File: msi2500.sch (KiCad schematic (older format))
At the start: 23 parts, among them J1 VCC_GPIO, J2 GPIO0, J3 GPIO1, J4 GPIO2, J5 GPIO3, U1 msi2500, Y1 24MHz, Y2 24MHZ

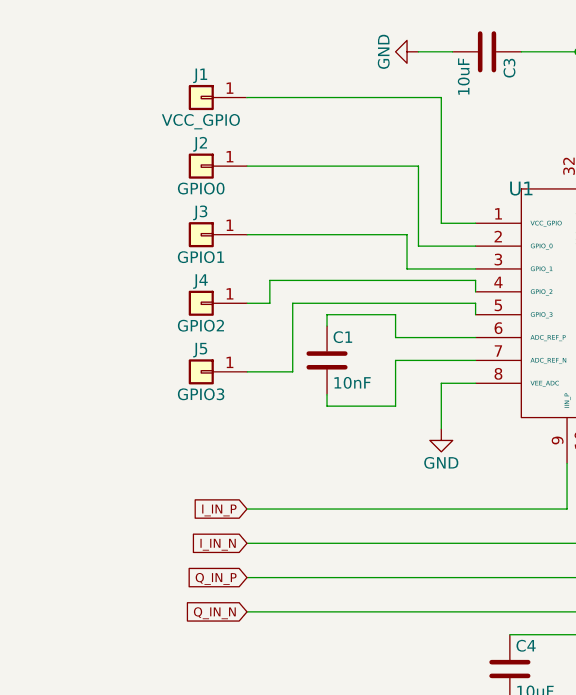
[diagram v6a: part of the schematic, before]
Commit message: add gpio pull down res
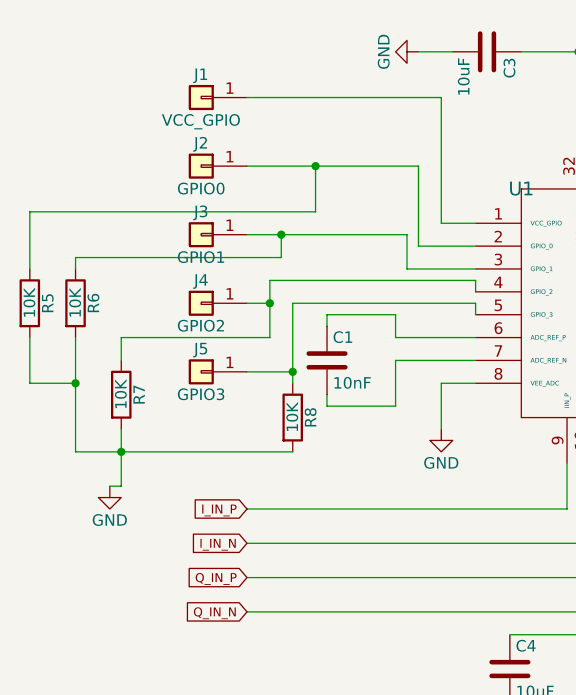
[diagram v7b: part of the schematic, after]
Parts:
- added R5, R6, R7, R8: 10K, Resistors_SMD:R_0603, symbol R
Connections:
- net GND: now also R5.2, R6.2, R7.2, R8.2
- net at J2.1 (Pin_1), U1.2 (GPIO_0): now also R5.1
- net at J3.1 (Pin_1), U1.3 (GPIO_1): now also R6.1
- net at J4.1 (Pin_1), U1.4 (GPIO_2): now also R7.1
- net at J5.1 (Pin_1), U1.5 (GPIO_3): now also R8.1
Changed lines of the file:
@@
 $EndDescr
 $Comp
-L GND #PWR5
+L GND #PWR6
 U 1 1 5C68D20C
 P 5450 2800
-F 0 "#PWR5" H 5450 2550 50  0001 C CNN
+F 0 "#PWR6" H 5450 2550 50  0001 C CNN
 F 1 "GND" H 5450 2650 50  0000 C CNN
 F 2 "" H 5450 2800 50  0001 C CNN
@@
 $EndComp
 $Comp
-L GND #PWR8
+L GND #PWR9
 U 1 1 5C68D2D4
 P 5900 4750
-F 0 "#PWR8" H 5900 4500 50  0001 C CNN
+F 0 "#PWR9" H 5900 4500 50  0001 C CNN
 F 1 "GND" H 5900 4600 50  0000 C CNN
 F 2 "" H 5900 4750 50  0001 C CNN
@@
 	4350 3950 4050 3950
 $Comp
-L GND #PWR3
+L GND #PWR4
 U 1 1 5C68D520
 P 4550 4450
-F 0 "#PWR3" H 4550 4200 50  0001 C CNN
+F 0 "#PWR4" H 4550 4200 50  0001 C CNN
 F 1 "GND" H 4550 4300 50  0000 C CNN
 F 2 "" H 4550 4450 50  0001 C CNN
@@
 	5800 5100 6950 5100
 $Comp
-L GND #PWR4
+L GND #PWR5
 U 1 1 5C68D665
 P 4850 5850
-F 0 "#PWR4" H 4850 5600 50  0001 C CNN
+F 0 "#PWR5" H 4850 5600 50  0001 C CNN
 F 1 "GND" H 4850 5700 50  0000 C CNN
 F 2 "" H 4850 5850 50  0001 C CNN
@@
 $EndComp
 $Comp
-L GND #PWR11
+L GND #PWR12
 U 1 1 5C68D681
 P 6950 5800
-F 0 "#PWR11" H 6950 5550 50  0001 C CNN
+F 0 "#PWR12" H 6950 5550 50  0001 C CNN
 F 1 "GND" H 6950 5650 50  0000 C CNN
 F 2 "" H 6950 5800 50  0001 C CNN
@@
 Connection ~ 5800 5600
 $Comp
-L GND #PWR6
+L GND #PWR7
 U 1 1 5C68DAB6
 P 5500 6150
-F 0 "#PWR6" H 5500 5900 50  0001 C CNN
+F 0 "#PWR7" H 5500 5900 50  0001 C CNN
 F 1 "GND" H 5500 6000 50  0000 C CNN
 F 2 "" H 5500 6150 50  0001 C CNN
@@
 $EndComp
 $Comp
-L GND #PWR7
+L GND #PWR8
 U 1 1 5C68DAD6
 P 5800 6150
-F 0 "#PWR7" H 5800 5900 50  0001 C CNN
+F 0 "#PWR8" H 5800 5900 50  0001 C CNN
 F 1 "GND" H 5800 6000 50  0000 C CNN
 F 2 "" H 5800 6150 50  0001 C CNN
@@
 VDIG
 $Comp
-L GND #PWR9
+L GND #PWR10
 U 1 1 5C68DD59
 P 6500 4700
-F 0 "#PWR9" H 6500 4450 50  0001 C CNN
+F 0 "#PWR10" H 6500 4450 50  0001 C CNN
 F 1 "GND" H 6500 4550 50  0000 C CNN
 F 2 "" H 6500 4700 50  0001 C CNN
@@
 $EndComp
 $Comp
-L GND #PWR10
+L GND #PWR11
 U 1 1 5C68DD79
 P 6800 4650
-F 0 "#PWR10" H 6800 4400 50  0001 C CNN
+F 0 "#PWR11" H 6800 4400 50  0001 C CNN
 F 1 "GND" H 6800 4500 50  0000 C CNN
 F 2 "" H 6800 4650 50  0001 C CNN
@@
 	6250 3950 7000 3950
 $Comp
-L GND #PWR12
+L GND #PWR13
 U 1 1 5C68E182
 P 7300 3800
-F 0 "#PWR12" H 7300 3550 50  0001 C CNN
+F 0 "#PWR13" H 7300 3550 50  0001 C CNN
 F 1 "GND" H 7300 3650 50  0000 C CNN
 F 2 "" H 7300 3800 50  0001 C CNN
@@
 $EndComp
 $Comp
-L GND #PWR14
+L GND #PWR15
 U 1 1 5C68E538
 P 7850 3200
-F 0 "#PWR14" H 7850 2950 50  0001 C CNN
+F 0 "#PWR15" H 7850 2950 50  0001 C CNN
 F 1 "GND" H 7850 3050 50  0000 C CNN
 F 2 "" H 7850 3200 50  0001 C CNN
@@
 $EndComp
 $Comp
-L GND #PWR15
+L GND #PWR16
 U 1 1 5C68E5AE
 P 7850 3600
-F 0 "#PWR15" H 7850 3350 50  0001 C CNN
+F 0 "#PWR16" H 7850 3350 50  0001 C CNN
 F 1 "GND" H 7850 3450 50  0000 C CNN
 F 2 "" H 7850 3600 50  0001 C CNN
@@
 Connection ~ 7100 3600
 $Comp
-L GND #PWR2
+L GND #PWR3
 U 1 1 5C68EA62
 P 4450 2800
-F 0 "#PWR2" H 4450 2550 50  0001 C CNN
+F 0 "#PWR3" H 4450 2550 50  0001 C CNN
 F 1 "GND" H 4450 2650 50  0000 C CNN
 F 2 "" H 4450 2800 50  0001 C CNN
@@
 $EndComp
 $Comp
-L GND #PWR1
+L GND #PWR2
 U 1 1 5C68F152
 P 4450 2050
-F 0 "#PWR1" H 4450 1800 50  0001 C CNN
+F 0 "#PWR2" H 4450 1800 50  0001 C CNN
 F 1 "GND" H 4450 1900 50  0000 C CNN
 F 2 "" H 4450 2050 50  0001 C CNN
@@
 	3700 3900 3800 3900
 Wire Wire Line
-	3800 3900 3800 3800
+	3800 3800 3800 4050
 Wire Wire Line
 	3800 3800 4700 3800
@@
 	4700 3900 3900 3900
 Wire Wire Line
-	3900 3900 3900 4200
+	3900 3900 3900 4250
 Wire Wire Line
 	3900 4200 3700 4200
@@
 	6550 2200 6950 2200
 $Comp
-L GND #PWR13
+L GND #PWR14
 U 1 1 5CAA05D3
 P 7650 2650
-F 0 "#PWR13" H 7650 2400 50  0001 C CNN
+F 0 "#PWR14" H 7650 2400 50  0001 C CNN
 F 1 "GND" H 7650 2500 50  0000 C CNN
 F 2 "" H 7650 2650 50  0001 C CNN
@@
 	8800 3650 8800 3900
 $Comp
-L GND #PWR16
+L GND #PWR17
 U 1 1 5CAA16D2
 P 8800 4450
-F 0 "#PWR16" H 8800 4200 50  0001 C CNN
+F 0 "#PWR17" H 8800 4200 50  0001 C CNN
 F 1 "GND" H 8800 4300 50  0000 C CNN
 F 2 "" H 8800 4450 50  0001 C CNN
@@
 Wire Wire Line
 	7100 3250 7100 3200
+$Comp
+L R R7
+U 1 1 5CC1C3E0
+P 3150 4300
+F 0 "R7" V 3230 4300 50  0000 C CNN
+F 1 "10K" V 3150 4300 50  0000 C CNN
+F 2 "Resistors_SMD:R_0603" V 3080 4300 50  0001 C CNN
+F 3 "" H 3150 4300 50  0001 C CNN
+	1    3150 4300
+	1    0    0    -1
+$EndComp
+$Comp
+L R R6
+U 1 1 5CC1C53B
+P 2950 3900
+F 0 "R6" V 3030 3900 50  0000 C CNN
+F 1 "10K" V 2950 3900 50  0000 C CNN
+F 2 "Resistors_SMD:R_0603" V 2880 3900 50  0001 C CNN
+F 3 "" H 2950 3900 50  0001 C CNN
+	1    2950 3900
+	1    0    0    -1
+$EndComp
+$Comp
+L R R5
+U 1 1 5CC1C59C
+P 2750 3900
+F 0 "R5" V 2830 3900 50  0000 C CNN
+F 1 "10K" V 2750 3900 50  0000 C CNN
+F 2 "Resistors_SMD:R_0603" V 2680 3900 50  0001 C CNN
+F 3 "" H 2750 3900 50  0001 C CNN
+	1    2750 3900
+	1    0    0    -1
+$EndComp
+Wire Wire Line
+	4000 3300 4000 3500
+Wire Wire Line
+	4000 3500 2750 3500
+Wire Wire Line
+	2750 3500 2750 3750
+Connection ~ 4000 3300
+Wire Wire Line
+	3850 3600 3850 3700
+Wire Wire Line
+	3850 3700 2950 3700
+Wire Wire Line
+	2950 3700 2950 3750
+Connection ~ 3850 3600
+Wire Wire Line
+	3800 4050 3150 4050
+Wire Wire Line
+	3150 4050 3150 4150
+Connection ~ 3800 3900
+$Comp
+L GND #PWR1
+U 1 1 5CC1CA03
+P 3100 4700
+F 0 "#PWR1" H 3100 4450 50  0001 C CNN
+F 1 "GND" H 3100 4550 50  0000 C CNN
+F 2 "" H 3100 4700 50  0001 C CNN
+F 3 "" H 3100 4700 50  0001 C CNN
+	1    3100 4700
+	1    0    0    -1
+$EndComp
+Wire Wire Line
+	3150 4450 3150 4700
+Wire Wire Line
+	2950 4050 2950 4550
+Wire Wire Line
+	2950 4550 3900 4550
+Wire Wire Line
+	2750 4050 2750 4250
+Wire Wire Line
+	2750 4250 2950 4250
+Connection ~ 2950 4250
+$Comp
+L R R8
+U 1 1 5CC1D62D
+P 3900 4400
+F 0 "R8" V 3980 4400 50  0000 C CNN
+F 1 "10K" V 3900 4400 50  0000 C CNN
+F 2 "Resistors_SMD:R_0603" V 3830 4400 50  0001 C CNN
+F 3 "" H 3900 4400 50  0001 C CNN
+	1    3900 4400
+	1    0    0    -1
+$EndComp
+Connection ~ 3900 4200
+Connection ~ 3150 4550
+Wire Wire Line
+	3150 4700 3100 4700
 $EndSCHEMATC

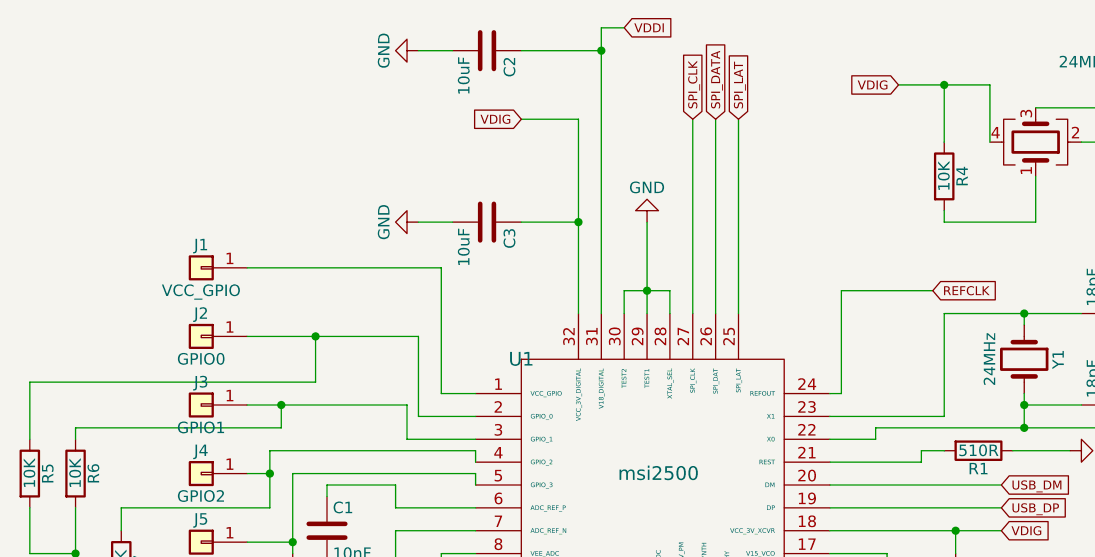
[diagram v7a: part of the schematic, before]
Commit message: fix bugs 1. not connect msi001 4 vcc to VRF 2. msi2500 VCC_GPIO connect to 1uF to GND 3. REF_CLK should use 10nF connect
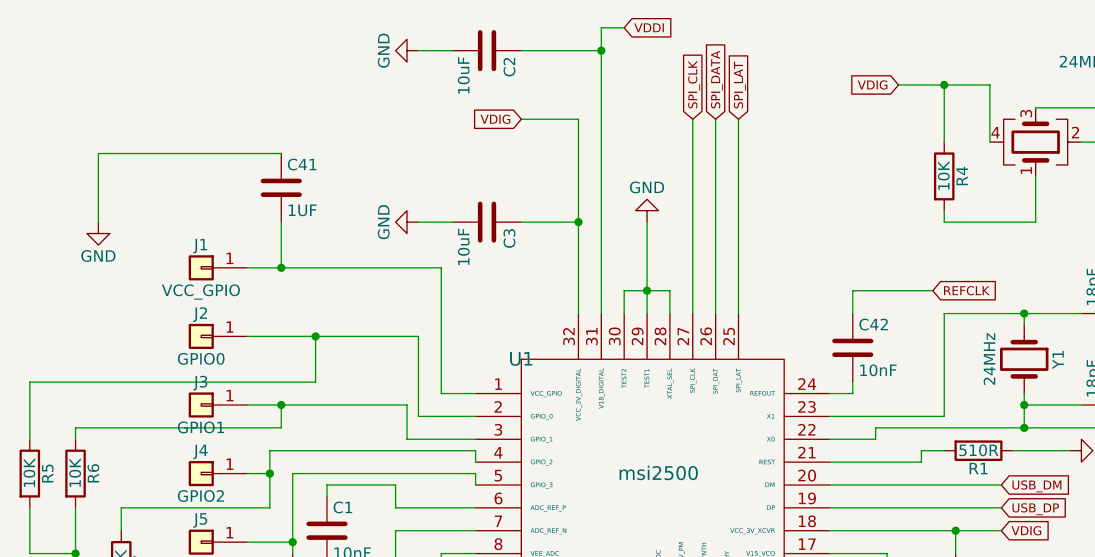
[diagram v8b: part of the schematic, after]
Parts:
- added C41: 1UF, Capacitors_SMD:C_0805, symbol C
- added C42: 10nF, Capacitors_SMD:C_0603, symbol C
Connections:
- net GND: now also C41.1
- net REFCLK: now also C42.1; no longer U1.24 (REFOUT)
- net at J1.1 (Pin_1), U1.1 (VCC_GPIO): now also C41.2
- new net: C42.2, U1.24 (REFOUT)
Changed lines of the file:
@@
 $EndDescr
 $Comp
-L GND #PWR6
+L GND #PWR7
 U 1 1 5C68D20C
 P 5450 2800
-F 0 "#PWR6" H 5450 2550 50  0001 C CNN
+F 0 "#PWR7" H 5450 2550 50  0001 C CNN
 F 1 "GND" H 5450 2650 50  0000 C CNN
 F 2 "" H 5450 2800 50  0001 C CNN
@@
 $EndComp
 $Comp
-L GND #PWR9
+L GND #PWR10
 U 1 1 5C68D2D4
 P 5900 4750
-F 0 "#PWR9" H 5900 4500 50  0001 C CNN
+F 0 "#PWR10" H 5900 4500 50  0001 C CNN
 F 1 "GND" H 5900 4600 50  0000 C CNN
 F 2 "" H 5900 4750 50  0001 C CNN
@@
 	4350 3950 4050 3950
 $Comp
-L GND #PWR4
+L GND #PWR5
 U 1 1 5C68D520
 P 4550 4450
-F 0 "#PWR4" H 4550 4200 50  0001 C CNN
+F 0 "#PWR5" H 4550 4200 50  0001 C CNN
 F 1 "GND" H 4550 4300 50  0000 C CNN
 F 2 "" H 4550 4450 50  0001 C CNN
@@
 	5800 5100 6950 5100
 $Comp
-L GND #PWR5
+L GND #PWR6
 U 1 1 5C68D665
 P 4850 5850
-F 0 "#PWR5" H 4850 5600 50  0001 C CNN
+F 0 "#PWR6" H 4850 5600 50  0001 C CNN
 F 1 "GND" H 4850 5700 50  0000 C CNN
 F 2 "" H 4850 5850 50  0001 C CNN
@@
 $EndComp
 $Comp
-L GND #PWR12
+L GND #PWR13
 U 1 1 5C68D681
 P 6950 5800
-F 0 "#PWR12" H 6950 5550 50  0001 C CNN
+F 0 "#PWR13" H 6950 5550 50  0001 C CNN
 F 1 "GND" H 6950 5650 50  0000 C CNN
 F 2 "" H 6950 5800 50  0001 C CNN
@@
 Connection ~ 5800 5600
 $Comp
-L GND #PWR7
+L GND #PWR8
 U 1 1 5C68DAB6
 P 5500 6150
-F 0 "#PWR7" H 5500 5900 50  0001 C CNN
+F 0 "#PWR8" H 5500 5900 50  0001 C CNN
 F 1 "GND" H 5500 6000 50  0000 C CNN
 F 2 "" H 5500 6150 50  0001 C CNN
@@
 $EndComp
 $Comp
-L GND #PWR8
+L GND #PWR9
 U 1 1 5C68DAD6
 P 5800 6150
-F 0 "#PWR8" H 5800 5900 50  0001 C CNN
+F 0 "#PWR9" H 5800 5900 50  0001 C CNN
 F 1 "GND" H 5800 6000 50  0000 C CNN
 F 2 "" H 5800 6150 50  0001 C CNN
@@
 VDIG
 $Comp
-L GND #PWR10
+L GND #PWR11
 U 1 1 5C68DD59
 P 6500 4700
-F 0 "#PWR10" H 6500 4450 50  0001 C CNN
+F 0 "#PWR11" H 6500 4450 50  0001 C CNN
 F 1 "GND" H 6500 4550 50  0000 C CNN
 F 2 "" H 6500 4700 50  0001 C CNN
@@
 $EndComp
 $Comp
-L GND #PWR11
+L GND #PWR12
 U 1 1 5C68DD79
 P 6800 4650
-F 0 "#PWR11" H 6800 4400 50  0001 C CNN
+F 0 "#PWR12" H 6800 4400 50  0001 C CNN
 F 1 "GND" H 6800 4500 50  0000 C CNN
 F 2 "" H 6800 4650 50  0001 C CNN
@@
 	6250 3950 7000 3950
 $Comp
-L GND #PWR13
+L GND #PWR14
 U 1 1 5C68E182
 P 7300 3800
-F 0 "#PWR13" H 7300 3550 50  0001 C CNN
+F 0 "#PWR14" H 7300 3550 50  0001 C CNN
 F 1 "GND" H 7300 3650 50  0000 C CNN
 F 2 "" H 7300 3800 50  0001 C CNN
@@
 REFCLK
 Wire Wire Line
-	6300 3100 6700 3100
+	6350 3100 6700 3100
 $Comp
 L Crystal Y1
@@
 $EndComp
 $Comp
-L GND #PWR15
+L GND #PWR16
 U 1 1 5C68E538
 P 7850 3200
-F 0 "#PWR15" H 7850 2950 50  0001 C CNN
+F 0 "#PWR16" H 7850 2950 50  0001 C CNN
 F 1 "GND" H 7850 3050 50  0000 C CNN
 F 2 "" H 7850 3200 50  0001 C CNN
@@
 $EndComp
 $Comp
-L GND #PWR16
+L GND #PWR17
 U 1 1 5C68E5AE
 P 7850 3600
-F 0 "#PWR16" H 7850 3350 50  0001 C CNN
+F 0 "#PWR17" H 7850 3350 50  0001 C CNN
 F 1 "GND" H 7850 3450 50  0000 C CNN
 F 2 "" H 7850 3600 50  0001 C CNN
@@
 Connection ~ 7100 3600
 $Comp
-L GND #PWR3
+L GND #PWR4
 U 1 1 5C68EA62
 P 4450 2800
-F 0 "#PWR3" H 4450 2550 50  0001 C CNN
+F 0 "#PWR4" H 4450 2550 50  0001 C CNN
 F 1 "GND" H 4450 2650 50  0000 C CNN
 F 2 "" H 4450 2800 50  0001 C CNN
@@
 $EndComp
 $Comp
-L GND #PWR2
+L GND #PWR3
 U 1 1 5C68F152
 P 4450 2050
-F 0 "#PWR2" H 4450 1800 50  0001 C CNN
+F 0 "#PWR3" H 4450 1800 50  0001 C CNN
 F 1 "GND" H 4450 1900 50  0000 C CNN
 F 2 "" H 4450 2050 50  0001 C CNN
@@
 	5400 5250 5400 4600
 Wire Wire Line
-	6300 3100 6300 3550
-Wire Wire Line
-	6300 3550 6250 3550
+	6250 3550 6350 3550
 Wire Wire Line
 	5650 3200 5650 2350
@@
 	6550 2200 6950 2200
 $Comp
-L GND #PWR14
+L GND #PWR15
 U 1 1 5CAA05D3
 P 7650 2650
-F 0 "#PWR14" H 7650 2400 50  0001 C CNN
+F 0 "#PWR15" H 7650 2400 50  0001 C CNN
 F 1 "GND" H 7650 2500 50  0000 C CNN
 F 2 "" H 7650 2650 50  0001 C CNN
@@
 	8800 3650 8800 3900
 $Comp
-L GND #PWR17
+L GND #PWR18
 U 1 1 5CAA16D2
 P 8800 4450
-F 0 "#PWR17" H 8800 4200 50  0001 C CNN
+F 0 "#PWR18" H 8800 4200 50  0001 C CNN
 F 1 "GND" H 8800 4300 50  0000 C CNN
 F 2 "" H 8800 4450 50  0001 C CNN
@@
 Connection ~ 3800 3900
 $Comp
-L GND #PWR1
+L GND #PWR2
 U 1 1 5CC1CA03
 P 3100 4700
-F 0 "#PWR1" H 3100 4450 50  0001 C CNN
+F 0 "#PWR2" H 3100 4450 50  0001 C CNN
 F 1 "GND" H 3100 4550 50  0000 C CNN
 F 2 "" H 3100 4700 50  0001 C CNN
@@
 Wire Wire Line
 	3150 4700 3100 4700
+$Comp
+L C C41
+U 1 1 5CD0470B
+P 3850 2650
+F 0 "C41" H 3875 2750 50  0000 L CNN
+F 1 "1UF" H 3875 2550 50  0000 L CNN
+F 2 "Capacitors_SMD:C_0805" H 3888 2500 50  0001 C CNN
+F 3 "" H 3850 2650 50  0001 C CNN
+	1    3850 2650
+	1    0    0    -1
+$EndComp
+$Comp
+L GND #PWR1
+U 1 1 5CD047D8
+P 3050 2800
+F 0 "#PWR1" H 3050 2550 50  0001 C CNN
+F 1 "GND" H 3050 2650 50  0000 C CNN
+F 2 "" H 3050 2800 50  0001 C CNN
+F 3 "" H 3050 2800 50  0001 C CNN
+	1    3050 2800
+	1    0    0    -1
+$EndComp
+Wire Wire Line
+	3850 2800 3850 3000
+Connection ~ 3850 3000
+Wire Wire Line
+	3850 2500 3050 2500
+Wire Wire Line
+	3050 2500 3050 2800
+$Comp
+L C C42
+U 1 1 5CD2D826
+P 6350 3350
+F 0 "C42" H 6375 3450 50  0000 L CNN
+F 1 "10nF" H 6375 3250 50  0000 L CNN
+F 2 "Capacitors_SMD:C_0603" H 6388 3200 50  0001 C CNN
+F 3 "" H 6350 3350 50  0001 C CNN
+	1    6350 3350
+	1    0    0    -1
+$EndComp
+Wire Wire Line
+	6350 3550 6350 3500
+Wire Wire Line
+	6350 3200 6350 3100
 $EndSCHEMATC
